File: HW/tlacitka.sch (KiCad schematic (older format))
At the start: 21 parts

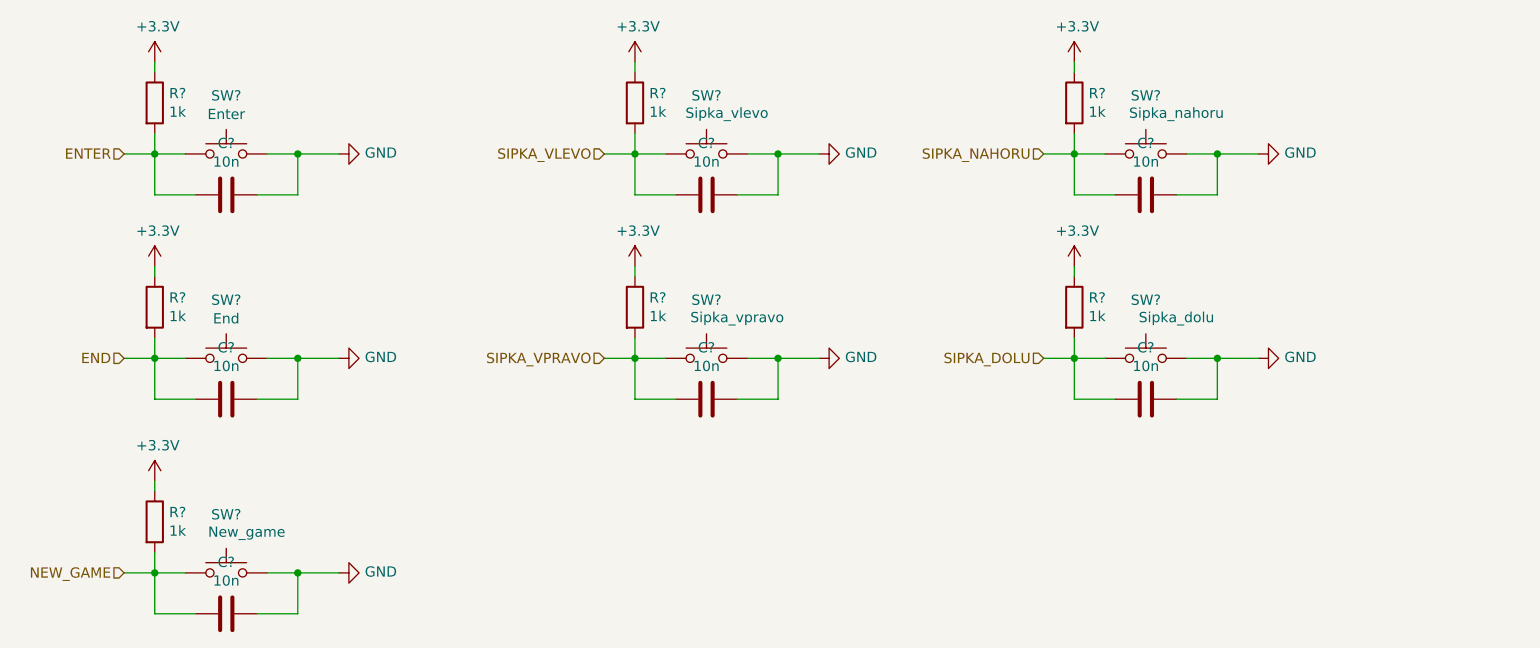
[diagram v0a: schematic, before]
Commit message: add power supply for ESP, erase resistors by buttons, add power supply for CP2102, add communication control (CP2102-ESP)
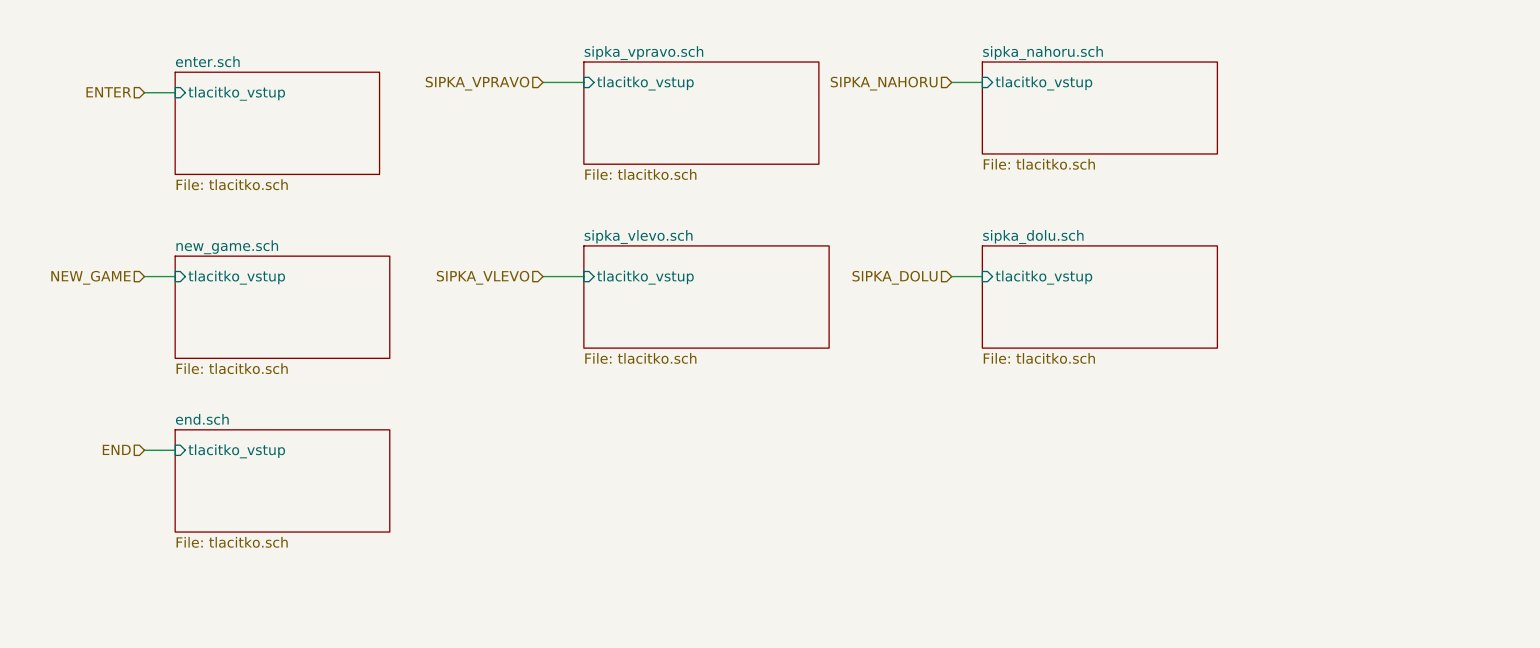
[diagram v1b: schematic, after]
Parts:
- removed C? (x7): 10n, Capacitor_SMD:C_0402_1005Metric, symbol Device:C
- removed R? (x7): 1k, Resistor_SMD:R_0402_1005Metric, symbol Device:R
- removed SW?: Enter, Button_Switch_THT:SW_Tactile_Straight_KSL0Axx1LFTR, symbol Switch:SW_Push
- removed SW?: End, Button_Switch_THT:SW_Tactile_Straight_KSL0Axx1LFTR, symbol Switch:SW_Push
- removed SW?: New_game, Button_Switch_THT:SW_Tactile_Straight_KSL0Axx1LFTR, symbol Switch:SW_Push
- removed SW?: Sipka_vlevo, Button_Switch_THT:SW_Tactile_Straight_KSL0Axx1LFTR, symbol Switch:SW_Push
- removed SW?: Sipka_vpravo, Button_Switch_THT:SW_Tactile_Straight_KSL0Axx1LFTR, symbol Switch:SW_Push
- removed SW?: Sipka_nahoru, Button_Switch_THT:SW_Tactile_Straight_KSL0Axx1LFTR, symbol Switch:SW_Push
- removed SW?: Sipka_dolu, Button_Switch_THT:SW_Tactile_Straight_KSL0Axx1LFTR, symbol Switch:SW_Push

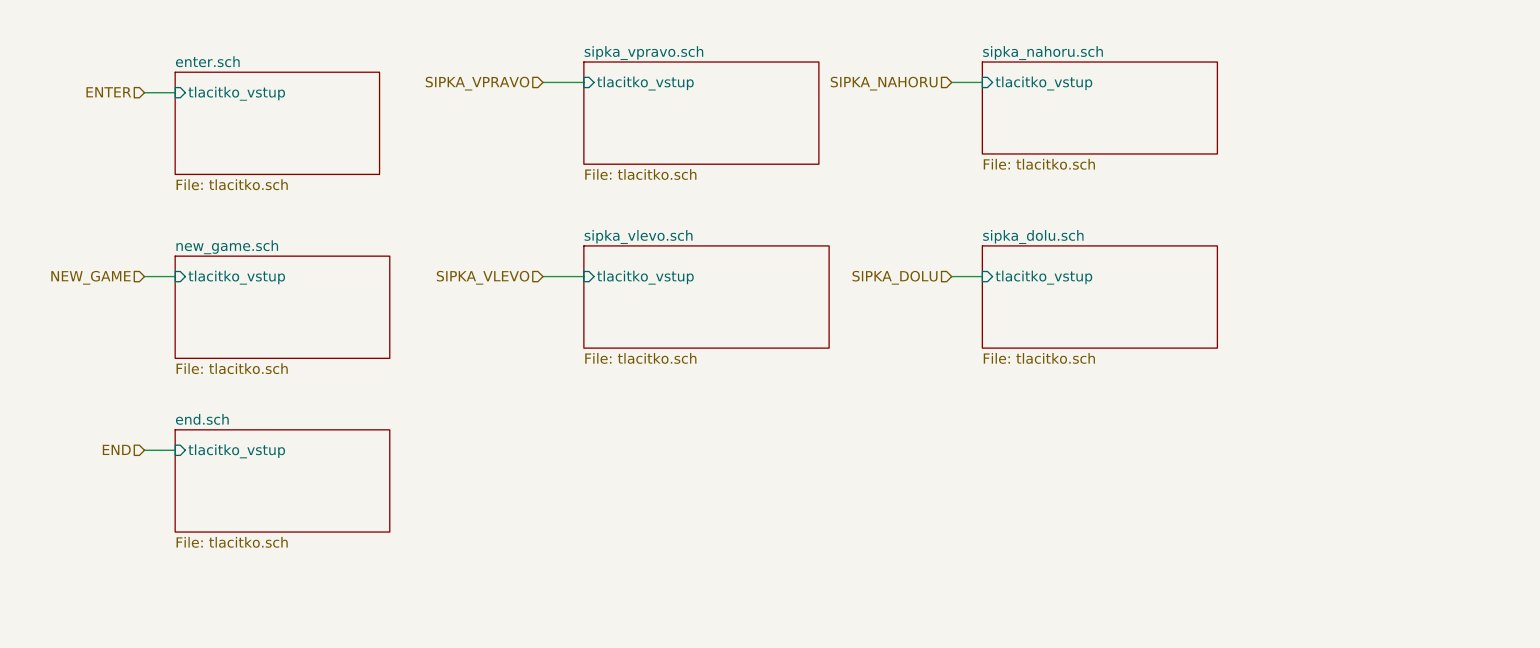
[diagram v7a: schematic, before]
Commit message: make smaller test version, start routing
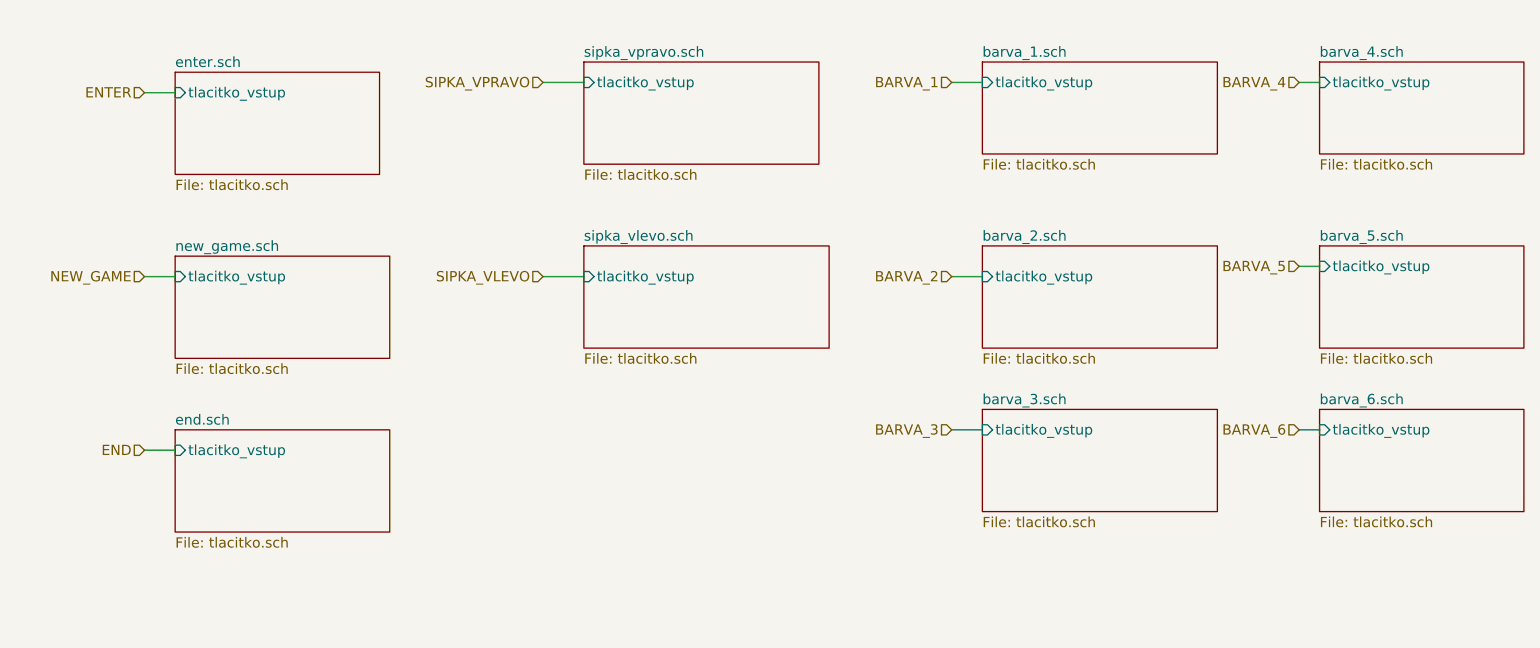
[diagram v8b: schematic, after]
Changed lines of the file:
@@
 $Descr A4 11693 8268
 encoding utf-8
-Sheet 3 44
+Sheet 3 34
 Title ""
 Date ""
@@
 S 5650 1050 1150 450
 U 5F76F2AA
-F0 "sipka_nahoru.sch" 50
+F0 "barva_1.sch" 50
 F1 "tlacitko.sch" 50
 F2 "tlacitko_vstup" I L 5650 1150 50
@@
 S 5650 1950 1150 500
 U 5F76F385
-F0 "sipka_dolu.sch" 50
+F0 "barva_2.sch" 50
 F1 "tlacitko.sch" 50
 F2 "tlacitko_vstup" I L 5650 2100 50
@@
 SIPKA_VLEVO
 Text HLabel 5500 1150 0    50   Input ~ 0
-SIPKA_NAHORU
+BARVA_1
 Text HLabel 5500 2100 0    50   Input ~ 0
-SIPKA_DOLU
+BARVA_2
 Wire Wire Line
 	5500 2100 5650 2100
@@
 Wire Wire Line
 	3700 2100 3500 2100
+$Sheet
+S 5650 2750 1150 500
+U 5F896DB4
+F0 "barva_3.sch" 50
+F1 "tlacitko.sch" 50
+F2 "tlacitko_vstup" I L 5650 2850 50
+$EndSheet
+$Sheet
+S 7300 1050 1000 450
+U 5F896DD0
+F0 "barva_4.sch" 50
+F1 "tlacitko.sch" 50
+F2 "tlacitko_vstup" I L 7300 1150 50
+$EndSheet
+$Sheet
+S 7300 1950 1000 500
+U 5F896DFE
+F0 "barva_5.sch" 50
+F1 "tlacitko.sch" 50
+F2 "tlacitko_vstup" I L 7300 2050 50
+$EndSheet
+$Sheet
+S 7300 2750 1000 500
+U 5F896E12
+F0 "barva_6.sch" 50
+F1 "tlacitko.sch" 50
+F2 "tlacitko_vstup" I L 7300 2850 50
+$EndSheet
+Text HLabel 5500 2850 0    50   Input ~ 0
+BARVA_3
+Text HLabel 7200 1150 0    50   Input ~ 0
+BARVA_4
+Text HLabel 7200 2050 0    50   Input ~ 0
+BARVA_5
+Text HLabel 7200 2850 0    50   Input ~ 0
+BARVA_6
+Wire Wire Line
+	7200 2850 7300 2850
+Wire Wire Line
+	7300 2050 7200 2050
+Wire Wire Line
+	7200 1150 7300 1150
+Wire Wire Line
+	5650 2850 5500 2850
 $EndSCHEMATC
